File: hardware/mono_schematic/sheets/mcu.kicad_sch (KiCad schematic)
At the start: 26 parts, among them SW1 KMR2, U1 ESP32-S3FN8, Y1 L327S400H11L

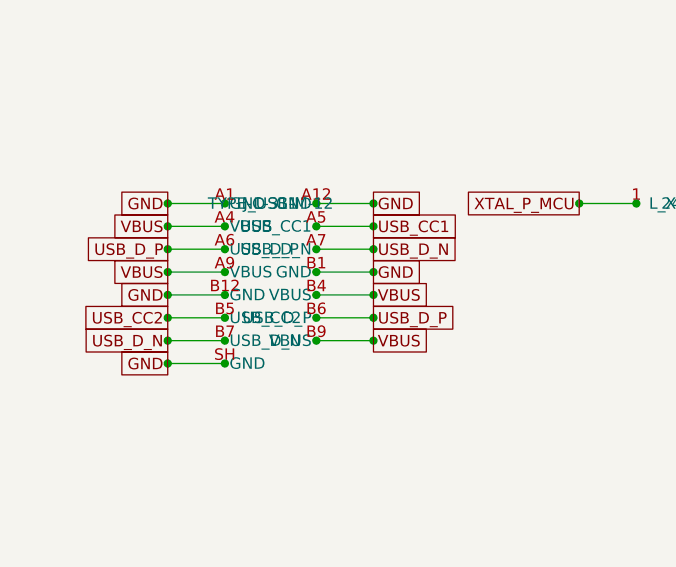
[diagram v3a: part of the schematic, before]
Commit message: mono_electronics v13 chunk2: USB input OVP — U_OVP1 TPS259531DSGR eFuse (5.7 V OV clamp, 1.17 A limit R_ILM1 1.78k, UVLO 4.28 V via 100k/39k), D_VBUS1 SMF12A TVS on VBUS_CONN; USBLC6 now on protected VBUS; schematic regen (ERC 0, 0 diffs); DRC 0/0/0
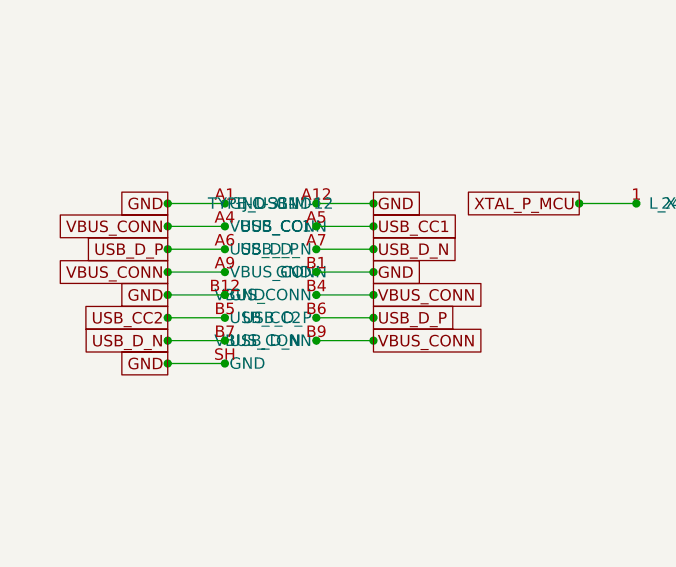
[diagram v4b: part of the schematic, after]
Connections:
- net VBUS: no longer J_USB1.A4 (VBUS), J_USB1.A9 (VBUS), J_USB1.B4 (VBUS), J_USB1.B9 (VBUS)
- new net VBUS_CONN: J_USB1.A4 (VBUS_CONN), J_USB1.A9 (VBUS_CONN), J_USB1.B4 (VBUS_CONN), J_USB1.B9 (VBUS_CONN)
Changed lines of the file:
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@@
     (instances
       (project "mono_electronics"
-        (path "/ef9ddef6-951a-4841-b92b-3942848f846d"
+        (path "/dbafe076-e207-4e74-8257-bdd1e1b3eb81"
           (reference "C_CHIP_PU1")
           (unit 1)
@@
     (instances
       (project "mono_electronics"
-        (path "/ef9ddef6-951a-4841-b92b-3942848f846d"
+        (path "/dbafe076-e207-4e74-8257-bdd1e1b3eb81"
           (reference "C_MCU1")
           (unit 1)
@@
     (instances
       (project "mono_electronics"
-        (path "/ef9ddef6-951a-4841-b92b-3942848f846d"
+        (path "/dbafe076-e207-4e74-8257-bdd1e1b3eb81"
           (reference "C_MCU_A2")
           (unit 1)
@@
     (instances
       (project "mono_electronics"
-        (path "/ef9ddef6-951a-4841-b92b-3942848f846d"
+        (path "/dbafe076-e207-4e74-8257-bdd1e1b3eb81"
           (reference "C_MCU_A3")
           (unit 1)
@@
     (instances
       (project "mono_electronics"
-        (path "/ef9ddef6-951a-4841-b92b-3942848f846d"
+        (path "/dbafe076-e207-4e74-8257-bdd1e1b3eb81"
           (reference "C_MCU_CPU1")
           (unit 1)
@@
     (instances
       (project "mono_electronics"
-        (path "/ef9ddef6-951a-4841-b92b-3942848f846d"
+        (path "/dbafe076-e207-4e74-8257-bdd1e1b3eb81"
           (reference "C_MCU_DA1")
           (unit 1)
@@
     (instances
       (project "mono_electronics"
-        (path "/ef9ddef6-951a-4841-b92b-3942848f846d"
+        (path "/dbafe076-e207-4e74-8257-bdd1e1b3eb81"
           (reference "C_MCU_DA2")
           (unit 1)
@@
     (instances
       (project "mono_electronics"
-        (path "/ef9ddef6-951a-4841-b92b-3942848f846d"
+        (path "/dbafe076-e207-4e74-8257-bdd1e1b3eb81"
           (reference "C_MCU_RTC1")
           (unit 1)
@@
     (instances
       (project "mono_electronics"
-        (path "/ef9ddef6-951a-4841-b92b-3942848f846d"
+        (path "/dbafe076-e207-4e74-8257-bdd1e1b3eb81"
           (reference "C_MCU_SPI1")
           (unit 1)
@@
     (instances
       (project "mono_electronics"
-        (path "/ef9ddef6-951a-4841-b92b-3942848f846d"
+        (path "/dbafe076-e207-4e74-8257-bdd1e1b3eb81"
           (reference "C_USB1")
           (unit 1)
@@
     (instances
       (project "mono_electronics"
-        (path "/ef9ddef6-951a-4841-b92b-3942848f846d"
+        (path "/dbafe076-e207-4e74-8257-bdd1e1b3eb81"
           (reference "C_XTAL1")
           (unit 1)
@@
     (instances
       (project "mono_electronics"
-        (path "/ef9ddef6-951a-4841-b92b-3942848f846d"
+        (path "/dbafe076-e207-4e74-8257-bdd1e1b3eb81"
           (reference "C_XTAL2")
           (unit 1)
@@
     (instances
       (project "mono_electronics"
-        (path "/ef9ddef6-951a-4841-b92b-3942848f846d"
+        (path "/dbafe076-e207-4e74-8257-bdd1e1b3eb81"
           (reference "J_USB1")
           (unit 1)
@@
     (instances
       (project "mono_electronics"
-        (path "/ef9ddef6-951a-4841-b92b-3942848f846d"
+        (path "/dbafe076-e207-4e74-8257-bdd1e1b3eb81"
           (reference "L_XTAL1")
           (unit 1)
@@
     (instances
       (project "mono_electronics"
-        (path "/ef9ddef6-951a-4841-b92b-3942848f846d"
+        (path "/dbafe076-e207-4e74-8257-bdd1e1b3eb81"
           (reference "R_BOOT0")
           (unit 1)
@@
     (instances
       (project "mono_electronics"
-        (path "/ef9ddef6-951a-4841-b92b-3942848f846d"
+        (path "/dbafe076-e207-4e74-8257-bdd1e1b3eb81"
           (reference "R_CC1")
           (unit 1)
@@
     (instances
       (project "mono_electronics"
-        (path "/ef9ddef6-951a-4841-b92b-3942848f846d"
+        (path "/dbafe076-e207-4e74-8257-bdd1e1b3eb81"
           (reference "R_CC2")
           (unit 1)
@@
     (instances
       (project "mono_electronics"
-        (path "/ef9ddef6-951a-4841-b92b-3942848f846d"
+        (path "/dbafe076-e207-4e74-8257-bdd1e1b3eb81"
           (reference "R_CHIP_PU1")
           (unit 1)
@@
     (instances
       (project "mono_electronics"
-        (path "/ef9ddef6-951a-4841-b92b-3942848f846d"
+        (path "/dbafe076-e207-4e74-8257-bdd1e1b3eb81"
           (reference "R_USB_N1")
           (unit 1)
@@
     (instances
       (project "mono_electronics"
-        (path "/ef9ddef6-951a-4841-b92b-3942848f846d"
+        (path "/dbafe076-e207-4e74-8257-bdd1e1b3eb81"
           (reference "R_USB_P1")
           (unit 1)
@@
     (instances
       (project "mono_electronics"
-        (path "/ef9ddef6-951a-4841-b92b-3942848f846d"
+        (path "/dbafe076-e207-4e74-8257-bdd1e1b3eb81"
           (reference "SW1")
           (unit 1)
@@
     (instances
       (project "mono_electronics"
-        (path "/ef9ddef6-951a-4841-b92b-3942848f846d"
+        (path "/dbafe076-e207-4e74-8257-bdd1e1b3eb81"
           (reference "TP1")
           (unit 1)
@@
     (instances
       (project "mono_electronics"
-        (path "/ef9ddef6-951a-4841-b92b-3942848f846d"
+        (path "/dbafe076-e207-4e74-8257-bdd1e1b3eb81"
           (reference "TP2")
           (unit 1)
@@
     (instances
       (project "mono_electronics"
-        (path "/ef9ddef6-951a-4841-b92b-3942848f846d"
+        (path "/dbafe076-e207-4e74-8257-bdd1e1b3eb81"
           (reference "U1")
           (unit 1)
@@
     (instances
       (project "mono_electronics"
-        (path "/ef9ddef6-951a-4841-b92b-3942848f846d"
+        (path "/dbafe076-e207-4e74-8257-bdd1e1b3eb81"
           (reference "U_ESD1")
           (unit 1)
@@
     (instances
       (project "mono_electronics"
-        (path "/ef9ddef6-951a-4841-b92b-3942848f846d"
+        (path "/dbafe076-e207-4e74-8257-bdd1e1b3eb81"
           (reference "Y1")
           (unit 1)
@@
     )
   )
-  (global_label "VBUS"
+  (global_label "VBUS_CONN"
     (shape passive)
     (at 24.13 205.74 180)
@@
     )
   )
-  (global_label "VBUS"
+  (global_label "VBUS_CONN"
     (shape passive)
     (at 24.13 210.82 180)
@@
     )
   )
-  (global_label "VBUS"
+  (global_label "VBUS_CONN"
     (shape passive)
     (at 46.99 213.36 0)
@@
     )
   )
-  (global_label "VBUS"
+  (global_label "VBUS_CONN"
     (shape passive)
     (at 46.99 218.44 0)
@@
   )
   (sheet_instances
-    (path "/ef9ddef6-951a-4841-b92b-3942848f846d"
+    (path "/dbafe076-e207-4e74-8257-bdd1e1b3eb81"
       (page "1")
     )
